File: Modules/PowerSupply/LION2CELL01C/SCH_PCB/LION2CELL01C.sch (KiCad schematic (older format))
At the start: 96 parts, among them J1 JUMP_4X2, J10 JUMP_2x1, J11 JUMP_2x1, J12 JUMP_2x1, J13 JUMP_4X2, J14 JUMP_2x1, J2 JUMP_2x1, J3 JUMP_2x1, J4 JUMP_2x1, J5 JUMP_2x1, J6 JUMP_2x1, J7 JUMP_4X2, J8 CONN1_1, J9 CONN1_1, P1 _, P2 _, P3 _, P4 _, Q1 IRLML6244, Q2 MMBF170LT1G, Q3 MMBF170LT1G, Q4 BSS83P, SW1 SW_PUSH, U1 BQ29209, U2 BQ24103, U3 BQ34Z100, U4 SN74HC164D

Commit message: 
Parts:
- added 1,1~A, 2A: FUSE, Mlab_F:2410, symbol FUSE
- BT1: symbol 2x18650_LION -> 2x18650_LION-RESCUE-LION2CELL01C
- C1, C11, C12, C13, C14, C15, C16, C17, C18, C3, C4, C6, C7, C8, C9: symbol C -> C-RESCUE-LION2CELL01C
- C5: value 100nF -> 330nF; symbol C -> C-RESCUE-LION2CELL01C
- D10, D11, D12, D13, D14, D3, D4, D5, D7, D8, D9: symbol LED -> LED-RESCUE-LION2CELL01C
- D6: symbol ZENER -> ZENER-RESCUE-LION2CELL01C
- R1: value 1K -> 160R; symbol R -> R-RESCUE-LION2CELL01C
- R10, R11, R12, R13, R14, R15, R16, R17, R18, R19, R20, R21, R22, R23, R25, R26, R27, R28, R29, R30, R31, R32, R33, R34, R4, R5, R6, R7, R8, R9: symbol R -> R-RESCUE-LION2CELL01C
- R2: value 1K -> 260R; symbol R -> R-RESCUE-LION2CELL01C
- R24: value divider.1% 25ppm -> 140k .1% 25ppm; symbol R -> R-RESCUE-LION2CELL01C
- R3: value 240R -> 100R; symbol R -> R-RESCUE-LION2CELL01C

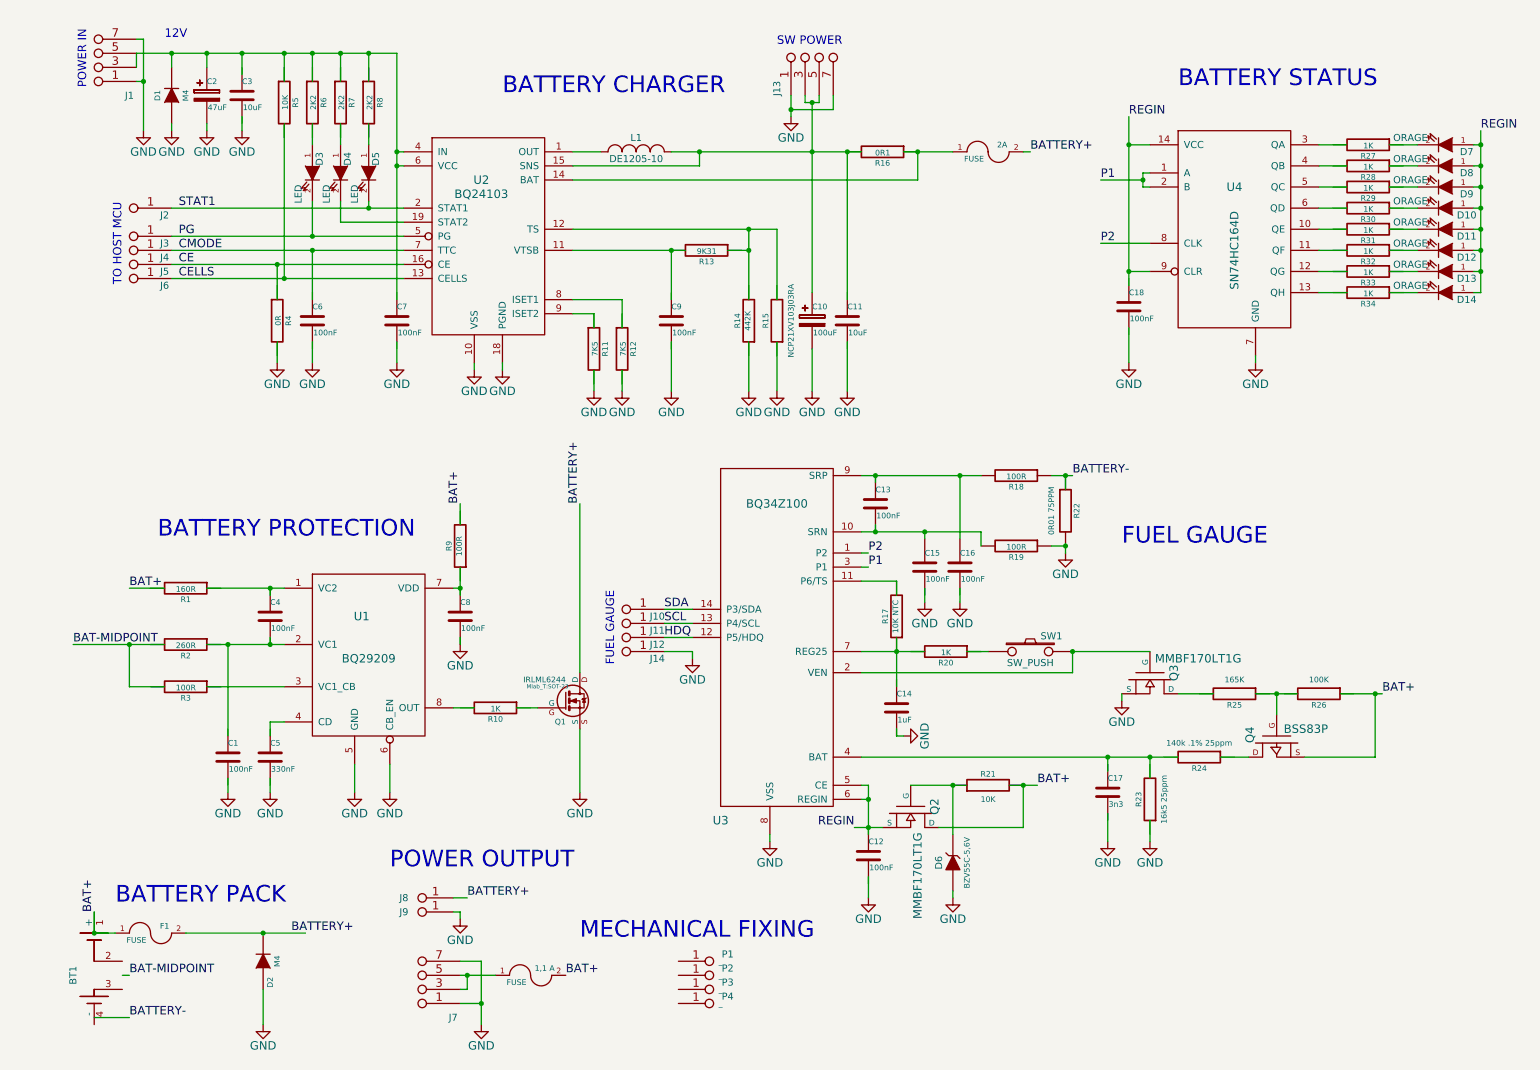
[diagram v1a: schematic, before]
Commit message: 
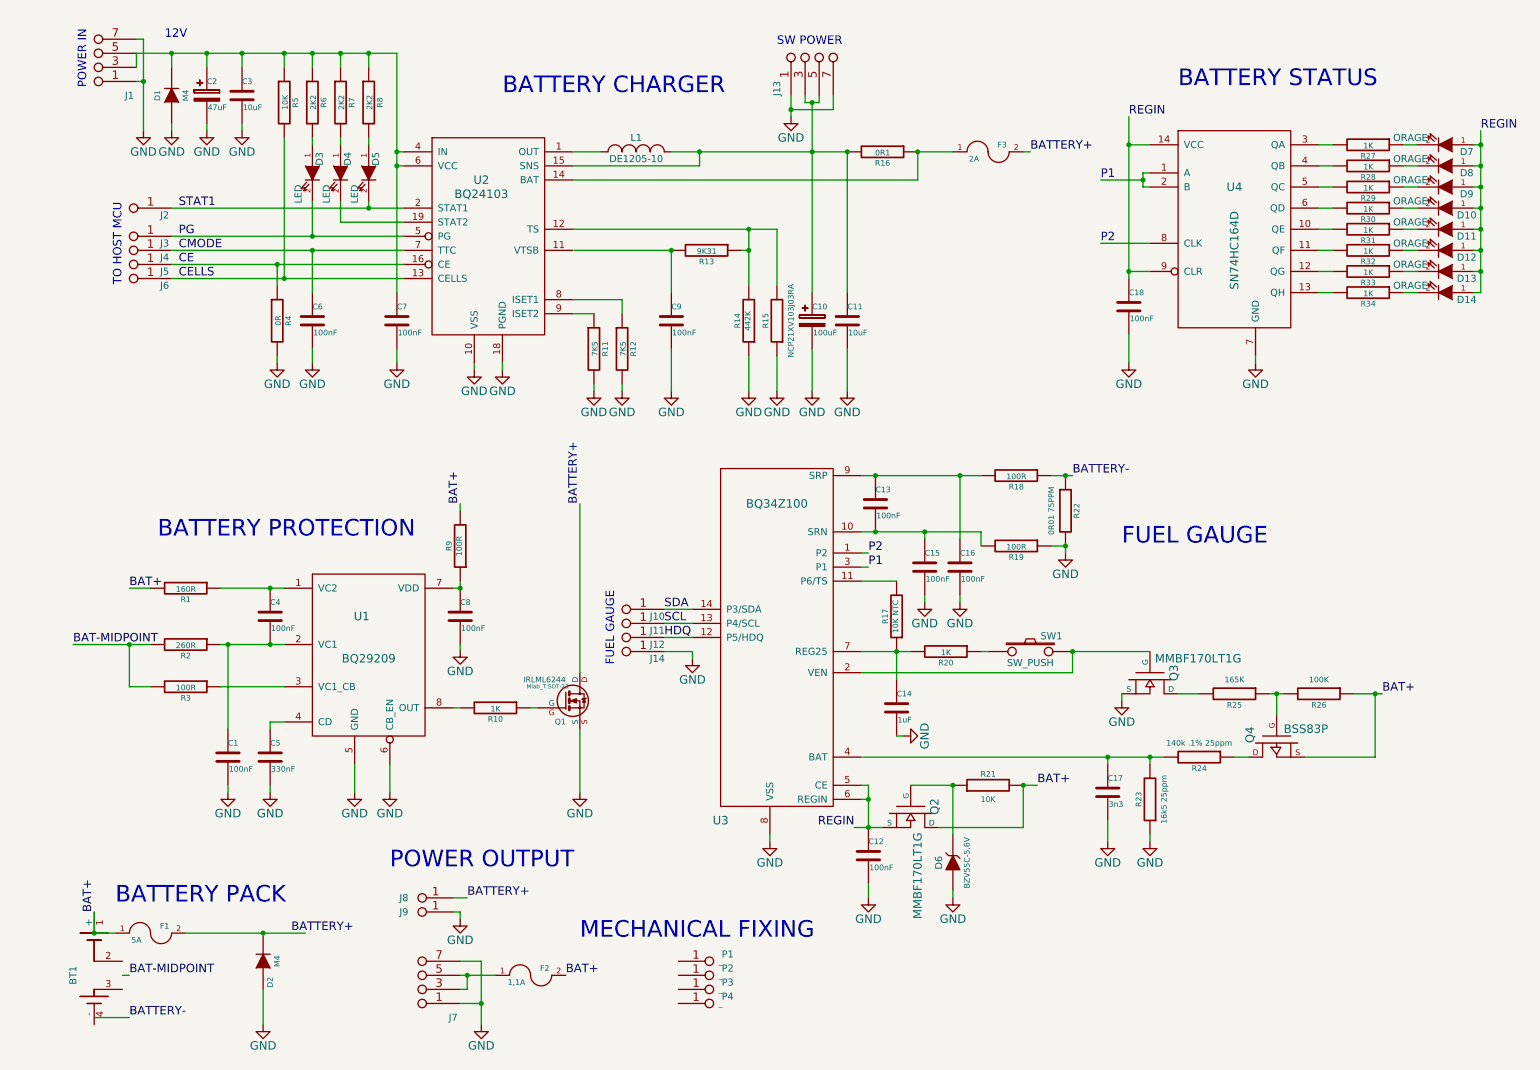
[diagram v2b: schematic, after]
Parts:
- F1: value FUSE -> 5A
- F2: renamed from 1,1~A; value FUSE -> 1,1A; footprint Mlab_F:2410 -> Mlab_F:1812
- F3: renamed from 2A; value FUSE -> 2A
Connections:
- wire segments 200 -> 194

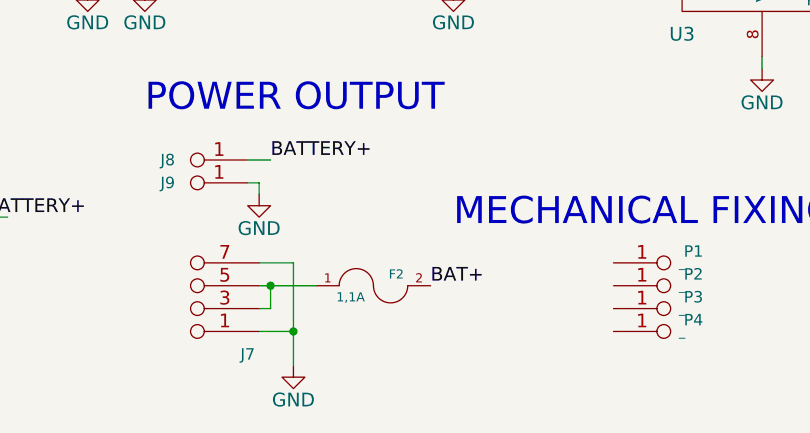
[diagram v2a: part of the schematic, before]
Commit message: 
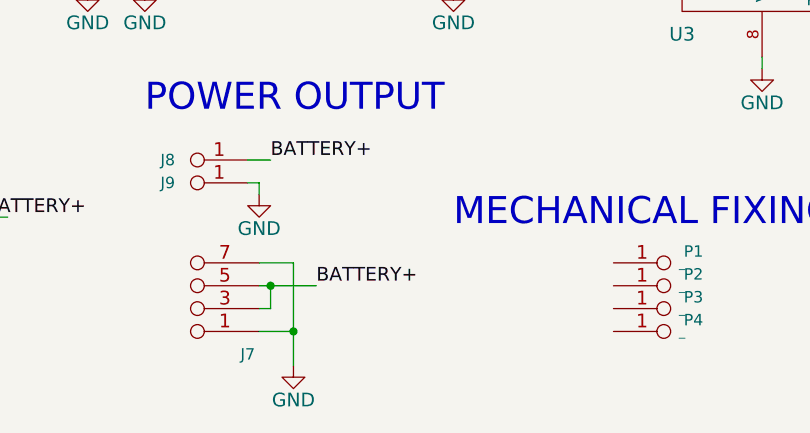
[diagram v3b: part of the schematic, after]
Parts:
- removed F2: 1,1A, Mlab_F:1812, symbol FUSE
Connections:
- net BATTERY+: now also J7.3 (4), J7.4, J7.5, J7.6 (5)
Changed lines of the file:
@@
 	1    0    0    -1
 $EndComp
-Text Label 4050 7250 0    60   ~ 0
-BAT+
 $Comp
 L GND #PWR035
@@
 $EndComp
 $Comp
-L FUSE F2
-U 1 1 563F69AE
-P 3800 7250
-F 0 "F2" H 3900 7300 40  0000 C CNN
-F 1 "1,1A" H 3700 7200 40  0000 C CNN
-F 2 "Mlab_F:1812" H 3800 7250 60  0001 C CNN
-F 3 "" H 3800 7250 60  0000 C CNN
-	1    3800 7250
-	1    0    0    -1
-$EndComp
-$Comp
 L R-RESCUE-LION2CELL01C R12
 U 1 1 553299F8
@@
 Wire Wire Line
 	1000 700  2850 700
+Text Label 3550 7250 0    60   ~ 0
+BATTERY+
 $EndSCHEMATC

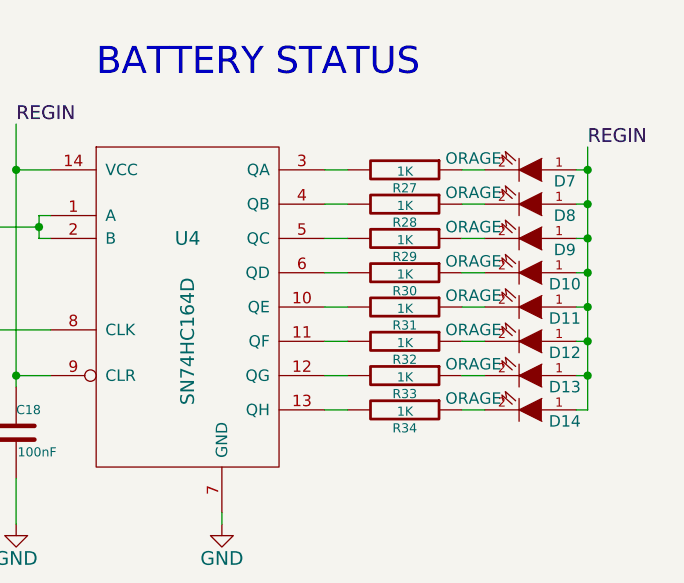
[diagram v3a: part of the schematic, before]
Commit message: 
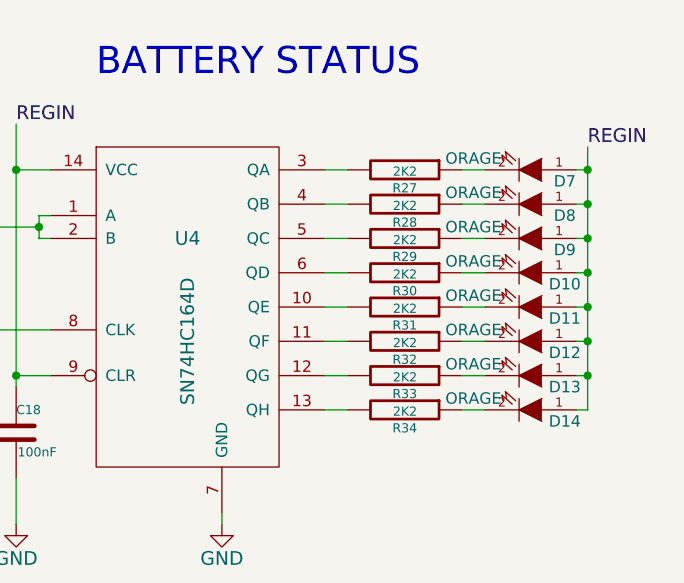
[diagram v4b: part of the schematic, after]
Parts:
- R27, R28, R29, R30, R31, R32, R33, R34: value 1K -> 2K2
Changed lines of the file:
@@
 P 9750 1350
 F 0 "R27" V 9830 1350 40  0000 C CNN
-F 1 "1K" V 9757 1351 40  0000 C CNN
+F 1 "2K2" V 9757 1351 40  0000 C CNN
 F 2 "Mlab_R:SMD-0805" V 9680 1350 30  0001 C CNN
 F 3 "" H 9750 1350 30  0000 C CNN
@@
 P 9750 1500
 F 0 "R28" V 9830 1500 40  0000 C CNN
-F 1 "1K" V 9757 1501 40  0000 C CNN
+F 1 "2K2" V 9757 1501 40  0000 C CNN
 F 2 "Mlab_R:SMD-0805" V 9680 1500 30  0001 C CNN
 F 3 "" H 9750 1500 30  0000 C CNN
@@
 P 9750 1650
 F 0 "R29" V 9830 1650 40  0000 C CNN
-F 1 "1K" V 9757 1651 40  0000 C CNN
+F 1 "2K2" V 9757 1651 40  0000 C CNN
 F 2 "Mlab_R:SMD-0805" V 9680 1650 30  0001 C CNN
 F 3 "" H 9750 1650 30  0000 C CNN
@@
 P 9750 1800
 F 0 "R30" V 9830 1800 40  0000 C CNN
-F 1 "1K" V 9757 1801 40  0000 C CNN
+F 1 "2K2" V 9757 1801 40  0000 C CNN
 F 2 "Mlab_R:SMD-0805" V 9680 1800 30  0001 C CNN
 F 3 "" H 9750 1800 30  0000 C CNN
@@
 P 9750 1950
 F 0 "R31" V 9830 1950 40  0000 C CNN
-F 1 "1K" V 9757 1951 40  0000 C CNN
+F 1 "2K2" V 9757 1951 40  0000 C CNN
 F 2 "Mlab_R:SMD-0805" V 9680 1950 30  0001 C CNN
 F 3 "" H 9750 1950 30  0000 C CNN
@@
 P 9750 2100
 F 0 "R32" V 9830 2100 40  0000 C CNN
-F 1 "1K" V 9757 2101 40  0000 C CNN
+F 1 "2K2" V 9757 2101 40  0000 C CNN
 F 2 "Mlab_R:SMD-0805" V 9680 2100 30  0001 C CNN
 F 3 "" H 9750 2100 30  0000 C CNN
@@
 P 9750 2250
 F 0 "R33" V 9830 2250 40  0000 C CNN
-F 1 "1K" V 9757 2251 40  0000 C CNN
+F 1 "2K2" V 9757 2251 40  0000 C CNN
 F 2 "Mlab_R:SMD-0805" V 9680 2250 30  0001 C CNN
 F 3 "" H 9750 2250 30  0000 C CNN
@@
 P 9750 2400
 F 0 "R34" V 9830 2400 40  0000 C CNN
-F 1 "1K" V 9757 2401 40  0000 C CNN
+F 1 "2K2" V 9757 2401 40  0000 C CNN
 F 2 "Mlab_R:SMD-0805" V 9680 2400 30  0001 C CNN
 F 3 "" H 9750 2400 30  0000 C CNN

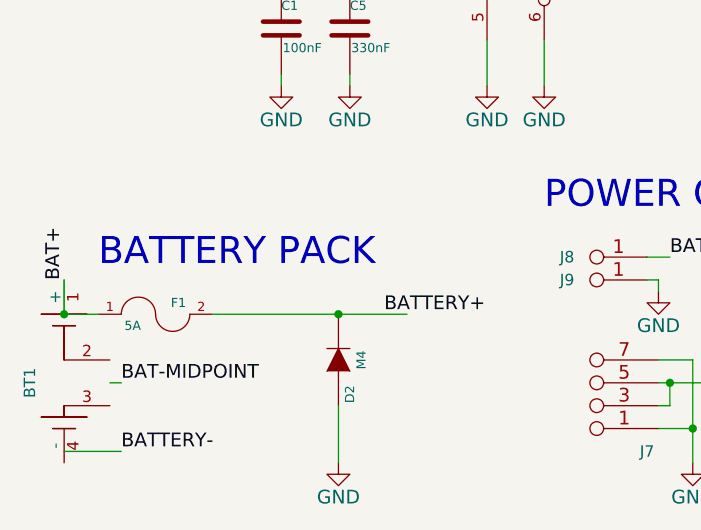
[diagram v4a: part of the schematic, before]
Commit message: Uprava LION2CELL01C. Generovani vyrobnich dat.
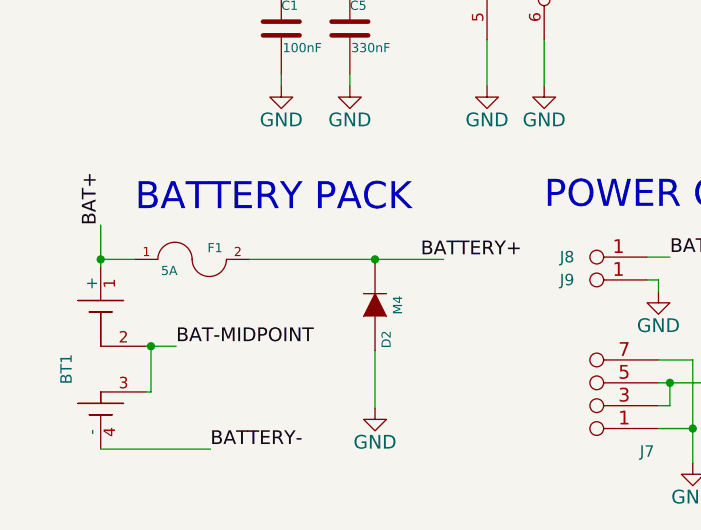
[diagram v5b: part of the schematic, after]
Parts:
- BT1: value 2x18650_LION -> 2x18650_LION-RESCUE-LION2CELL01C
- F1, F3: footprint Mlab_F:2410 -> Mlab_F:Drzak_2410
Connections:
- net BAT-MIDPOINT: now also BT1.2, BT1.3
- net BATTERY-: now also BT1.4 (-)
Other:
- moved on the sheet: D2, F1
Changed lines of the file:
@@
 BATTERY+
-$Comp
-L 2x18650_LION-RESCUE-LION2CELL01C BT1
-U 1 1 5532C7C3
-P 700 7250
-F 0 "BT1" V 550 7250 50  0000 C CNN
-F 1 "2x18650_LION" V 450 7250 50  0001 C CNN
-F 2 "Mlab_Batery:2LION" H 2300 7600 60  0001 C CNN
-F 3 "" H 2300 7600 60  0000 C CNN
-	1    700  7250
-	1    0    0    -1
-$EndComp
 $Comp
 L FUSE F1
 U 1 1 5532CA08
-P 1100 6950
-F 0 "F1" H 1200 7000 40  0000 C CNN
-F 1 "5A" H 1000 6900 40  0000 C CNN
-F 2 "Mlab_F:2410" H 1100 6950 60  0001 C CNN
-F 3 "" H 1100 6950 60  0000 C CNN
-	1    1100 6950
+P 1260 6710
+F 0 "F1" H 1360 6760 40  0000 C CNN
+F 1 "5A" H 1160 6660 40  0000 C CNN
+F 2 "Mlab_F:Drzak_2410" H 1260 6710 60  0001 C CNN
+F 3 "" H 1260 6710 60  0000 C CNN
+	1    1260 6710
 	1    0    0    -1
 $EndComp
@@
 L DIODE D2
 U 1 1 5532D00E
-P 1900 7150
-F 0 "D2" H 1750 7100 40  0000 C CNN
-F 1 "M4" H 1900 7050 40  0000 C CNN
-F 2 "Mlab_D:SMA_Standard" H 1900 7150 60  0001 C CNN
-F 3 "" H 1900 7150 60  0000 C CNN
-	1    1900 7150
+P 2060 6910
+F 0 "D2" H 1910 6860 40  0000 C CNN
+F 1 "M4" H 2060 6810 40  0000 C CNN
+F 2 "Mlab_D:SMA_Standard" H 2060 6910 60  0001 C CNN
+F 3 "" H 2060 6910 60  0000 C CNN
+	1    2060 6910
 	0    -1   -1   0
 $EndComp
@@
 L GND #PWR016
 U 1 1 5532D5CF
-P 1900 7600
-F 0 "#PWR016" H 1900 7350 60  0001 C CNN
-F 1 "GND" H 1900 7450 60  0000 C CNN
-F 2 "" H 1900 7600 60  0000 C CNN
-F 3 "" H 1900 7600 60  0000 C CNN
-	1    1900 7600
-	1    0    0    -1
-$EndComp
-Text Label 2100 6950 0    60   ~ 0
+P 2060 7360
+F 0 "#PWR016" H 2060 7110 60  0001 C CNN
+F 1 "GND" H 2060 7210 60  0000 C CNN
+F 2 "" H 2060 7360 60  0000 C CNN
+F 3 "" H 2060 7360 60  0000 C CNN
+	1    2060 7360
+	1    0    0    -1
+$EndComp
+Text Label 2260 6710 0    60   ~ 0
 BATTERY+
-Text Label 950  7250 0    60   ~ 0
+Text Label 1190 7090 0    60   ~ 0
 BAT-MIDPOINT
-Text Notes 850  6750 0    118  ~ 0
+Text Notes 1010 6510 0    118  ~ 0
 BATTERY PACK
 Text Notes 3600 1000 0    118  ~ 0
@@
 	1    0    0    -1
 $EndComp
-Text Label 950  7550 0    60   ~ 0
+Text Label 1340 7540 0    60   ~ 0
 BATTERY-
-Text Label 700  6800 1    60   ~ 0
+Text Label 860  6560 1    60   ~ 0
 BAT+
 $Comp
@@
 F 0 "F3" H 7150 1450 40  0000 C CNN
 F 1 "2A" H 6950 1350 40  0000 C CNN
-F 2 "Mlab_F:2410" H 7050 1400 60  0001 C CNN
+F 2 "Mlab_F:Drzak_2410" H 7050 1400 60  0001 C CNN
 F 3 "" H 7050 1400 60  0000 C CNN
 	1    7050 1400
@@
 Connection ~ 5650 1100
 Wire Wire Line
-	1900 7600 1900 7350
-Wire Wire Line
-	1350 6950 2200 6950
-Wire Wire Line
-	850  6950 700  6950
-Wire Wire Line
-	700  7550 950  7550
-Wire Wire Line
-	700  6950 700  6800
+	2060 7360 2060 7110
+Wire Wire Line
+	1510 6710 2360 6710
+Wire Wire Line
+	1010 6710 860  6710
+Wire Wire Line
+	860  7540 1340 7540
+Wire Wire Line
+	860  6560 860  6740
 Connection ~ 1950 4500
 Connection ~ 1950 4900
@@
 Connection ~ 6050 1400
 Connection ~ 7600 3700
-Connection ~ 1900 6950
+Connection ~ 2060 6710
 Wire Wire Line
 	4750 4650 4950 4650
@@
 Connection ~ 7300 5900
 Wire Wire Line
-	950  7250 900  7250
+	1060 7090 1190 7090
 Wire Wire Line
 	7350 1400 7300 1400
-Connection ~ 700  6950
+Connection ~ 860  6710
 Connection ~ 7650 4950
 Wire Wire Line
@@
 Text Label 3550 7250 0    60   ~ 0
 BATTERY+
+$Comp
+L 2x18650_LION-RESCUE-LION2CELL01C BT1
+U 1 1 564C3067
+P 860 7190
+F 0 "BT1" V 710 7190 50  0000 C CNN
+F 1 "2x18650_LION-RESCUE-LION2CELL01C" V 610 7190 50  0001 C CNN
+F 2 "Mlab_Batery:2LION" H 2460 7540 60  0001 C CNN
+F 3 "" H 2460 7540 60  0000 C CNN
+	1    860  7190
+	1    0    0    -1
+$EndComp
+Wire Wire Line
+	1060 7290 1080 7290
+Wire Wire Line
+	1080 7290 1080 7090
+Connection ~ 1080 7090
 $EndSCHEMATC

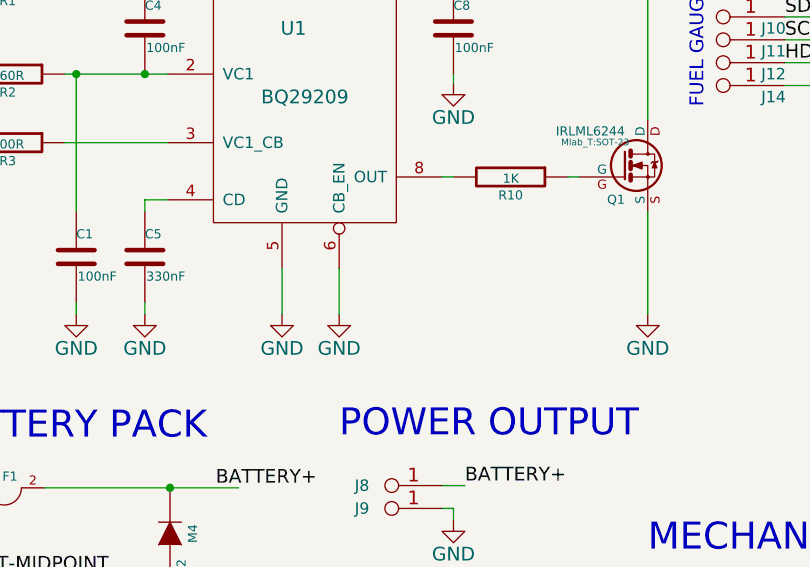
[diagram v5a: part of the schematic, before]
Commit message: 
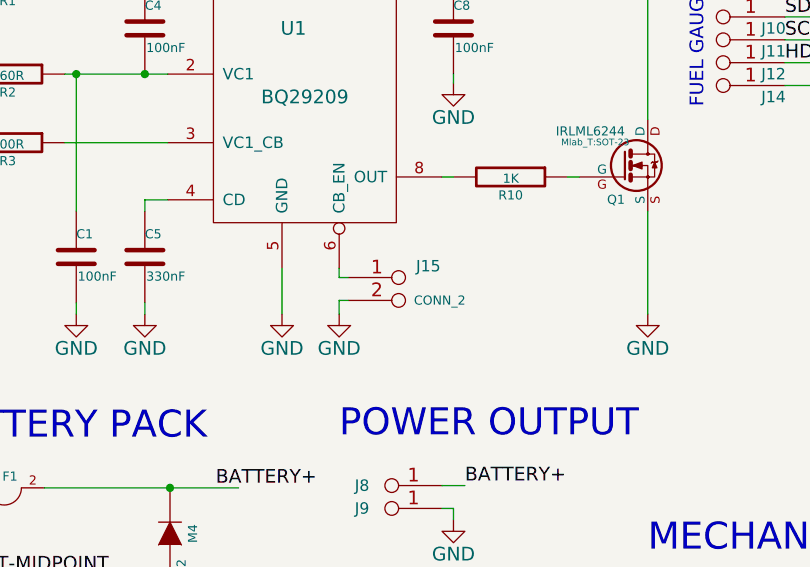
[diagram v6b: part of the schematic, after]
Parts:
- added J15: CONN_2, Mlab_Pin_Headers:SMD_1_2x2, symbol CONN_2
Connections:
- net GND: now also J15.2 (PM); no longer U1.6 (CB_EN)
- new net: J15.1 (P1), U1.6 (CB_EN)
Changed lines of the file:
@@
 	2550 5950 2550 5750
-Wire Wire Line
-	2800 5950 2800 5750
 Wire Wire Line
 	3250 4500 3300 4500
@@
 	1080 7290 1080 7090
 Connection ~ 1080 7090
+$Comp
+L CONN_2 J15
+U 1 1 566001CC
+P 3140 5840
+F 0 "J15" H 3190 5940 50  0000 C CNN
+F 1 "CONN_2" H 3240 5790 40  0000 C CNN
+F 2 "Mlab_Pin_Headers:SMD_1_2x2" H 3190 5790 60  0001 C CNN
+F 3 "" H 3190 5790 60  0000 C CNN
+	1    3140 5840
+	1    0    0    -1
+$EndComp
+Wire Wire Line
+	2800 5950 2800 5890
+Wire Wire Line
+	2800 5890 2840 5890
+Wire Wire Line
+	2840 5790 2800 5790
+Wire Wire Line
+	2800 5790 2800 5750
 $EndSCHEMATC
